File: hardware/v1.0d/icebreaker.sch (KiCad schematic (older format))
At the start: 133 parts, among them J1 Jumper, J10 Jumper, J11 Jumper, J12 Jumper, J13 Jumper, J14 Jumper, J15 Jumper, J16 Jumper, J17 Jumper, J18 Jumper, J19 Jumper, J2 Jumper, J20 Flash, J21 PMOD, J22 PMOD, J23 PMOD, J24 PMOD, J25 RGB Led, J26 5V AUX, J27 5V AUX, J28 CRESET, J29 Jumper, J3 Jumper, J30 Jumper, J31 RGB Led, J32 WS2812, J33 RGB Led, J34 SADD, J4 Jumper, J5 Jumper, J6 Jumper, J7 Jumper, J8 Jumper, J9 Jumper, P1 pkl_USB_OTG, P2 UP, P3 UP, P4 UP, P5 UP, P6 RAM_CS, Q1 BSS138, SW1 TACT, SW2 TACT, SW3 TACT, SW4 TACT, U1 93C46B-SOT-23-6, U2 3.3V, U3 1V2, U4 FT2232H, U5 W25Q, U6 ICE5LP4K-SG48, U7 12MHz

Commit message: Fixed RGB LED labling. Replaced RGB LED signals to be color agnostic.
The FPGA does not care which color is connected to which pin, so
referring to the pins as red, green and blue is bit silly. The signals
are now RGB0-2 instead. The only place where we label the colors are on
the actual Cree LED package pins.

This fixes #22
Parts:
- D11: symbol Device:LED_RGB -> pkl_device:LED_BGR; MFN (none) -> CLX6F-FKC; Manufacturer (none) -> Cree
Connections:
- net ~LED_BLU renamed ~LED_RGB0
- net ~LED_GRN renamed ~LED_RGB1
- net ~LED_RED renamed ~LED_RGB2
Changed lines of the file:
@@
 	10600 4100 10800 4100
 Text Label 10800 4100 0    50   ~ 0
-~LED_BLU
+~LED_RGB0
 Text Label 10800 4000 0    50   ~ 0
-~LED_GRN
+~LED_RGB1
 Text Label 10800 3900 0    50   ~ 0
-~LED_RED
+~LED_RGB2
 Text Notes 600  1700 0    100  ~ 0
 FTDI Programmer/UART/FIFO
@@
 Wire Wire Line
 	14700 8600 14300 8600
-Text Label 15600 8600 0    50   ~ 0
-~LED_RED
 Text Label 14300 8600 2    50   ~ 0
-~LED_GRN
+~LED_RGB1
+Text Label 15600 8600 0    50   ~ 0
+~LED_RGB2
 Text Label 15600 8700 0    50   ~ 0
-~LED_BLU
+~LED_RGB0
 Wire Wire Line
 	13300 4400 13500 4400
@@
 RAM CS
 $Comp
-L Device:LED_RGB D11
+L pkl_device:LED_BGR D11
 U 1 1 5C0C5D9F
 P 14950 9500
@@
 F 3 "~" H 14950 9450 50  0001 C CNN
 F 4 "YES" H 14950 9500 50  0001 C CNN "DNP"
+F 5 "Cree" H 14950 9500 50  0001 C CNN "Manufacturer"
+F 6 "CLX6F-FKC" H 14950 9500 50  0001 C CNN "MFN"
 	1    14950 9500
 	-1   0    0    -1
@@
 	15150 9700 15250 9700
 Text Label 15250 9300 0    50   ~ 0
-~LED_RED
+~LED_RGB2
 Text Label 15250 9500 0    50   ~ 0
-~LED_GRN
+~LED_RGB1
 Text Label 15250 9700 0    50   ~ 0
-~LED_BLU
+~LED_RGB0
 $Comp
 L pkl_misc:pkl_double_jumper_ncno J30

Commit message: Changed the VPP_2V5 diode footprint to SOD-523.
The SOD-523 is more common. While I was at it I also named the VPP_2V5
net.

This fixes #26
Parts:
- D2: value CDBU0520 -> ~~800mVf; footprint pkl_dipol:D_0603 -> pkl_dipol:D_SOD-523; Key diode-schottky-0603 -> diode-schottky-sod523
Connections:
- net VPP_2V5: now reaches C35.1, D2.C, U6.24 (VPP_2V5)
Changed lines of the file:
@@
 Text Label 10700 5700 0    50   ~ 0
 iCE_CRESET
-$Comp
-L pkl_device:pkl_Diode_Small D2
-U 1 1 5A83A5CC
-P 8150 5800
-F 0 "D2" H 8050 5750 50  0000 C CNN
-F 1 "CDBU0520" H 8400 5850 50  0000 C CNN
-F 2 "pkl_dipol:D_0603" V 8150 5800 60  0001 C CNN
-F 3 "" V 8150 5800 60  0000 C CNN
-F 4 "diode-schottky-0603" H 0   0   50  0001 C CNN "Key"
-F 5 "ANY" H 8150 5800 50  0001 C CNN "Source"
-	1    8150 5800
-	1    0    0    -1
-$EndComp
 Wire Wire Line
 	8250 5800 8350 5800
@@
 Text Notes 15250 9850 0    75   ~ 0
 Unpopulated
+$Comp
+L pkl_device:pkl_Diode_Small D2
+U 1 1 5A83A5CC
+P 8150 5800
+F 0 "D2" H 8000 5750 50  0000 L CNN
+F 1 "~~800mVf" H 8000 5650 50  0000 L CNN
+F 2 "pkl_dipol:D_SOD-523" V 8150 5800 60  0001 C CNN
+F 3 "" V 8150 5800 60  0000 C CNN
+F 4 "diode-schottky-sod523" H 0   0   50  0001 C CNN "Key"
+F 5 "ANY" H 8150 5800 50  0001 C CNN "Source"
+	1    8150 5800
+	1    0    0    -1
+$EndComp
+Text Label 8600 5800 2    50   ~ 0
+VPP_2V5
 $EndSCHEMATC

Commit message: Corrected the SAO/I2C ear name in schematic and on board.
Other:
- note added: "SAO/I2C "Ear""
- note removed: "SADD "Ear""
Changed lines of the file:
@@
 WS2812 "Ear"
 Text Notes 9600 10200 0    100  ~ 0
-SADD "Ear"
+SAO/I2C "Ear"
 Wire Notes Line
 	9500 10000 11700 10000

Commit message: Changed the AUX CS jumper to be Normally Closed.
This closes #28
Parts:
- J29: footprint pkl_jumpers:J_0603 -> pkl_jumpers:J_NC_0603_15; symbol pkl_misc:pkl_jumper -> pkl_misc:pkl_jumper_nc
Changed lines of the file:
@@
 $EndComp
 $Comp
-L pkl_misc:pkl_jumper J29
+L pkl_misc:pkl_jumper_nc J29
 U 1 1 5BF627F5
 P 5600 3550
 F 0 "J29" H 5450 3600 60  0000 C CNN
 F 1 "Jumper" H 5600 3695 60  0001 C CNN
-F 2 "pkl_jumpers:J_0603" H 5600 3550 60  0001 C CNN
+F 2 "pkl_jumpers:J_NC_0603_15" H 5600 3550 60  0001 C CNN
 F 3 "" H 5600 3550 60  0000 C CNN
 F 4 "ANY" H 5600 3550 50  0001 C CNN "Source"

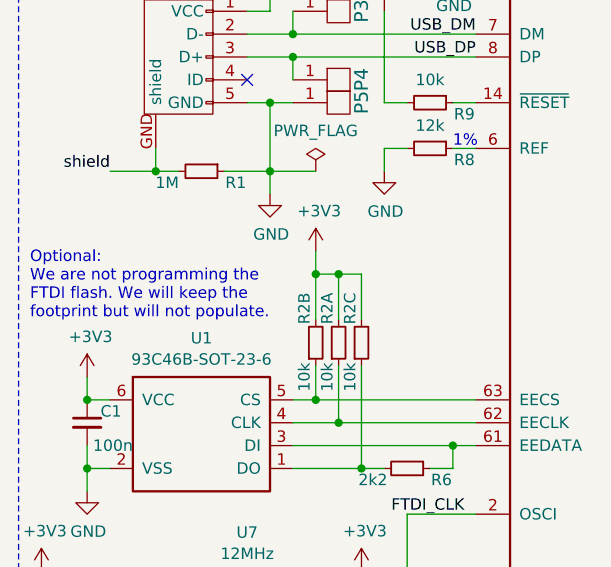
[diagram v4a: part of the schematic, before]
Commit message: Corrected the note about FTDI Flash.
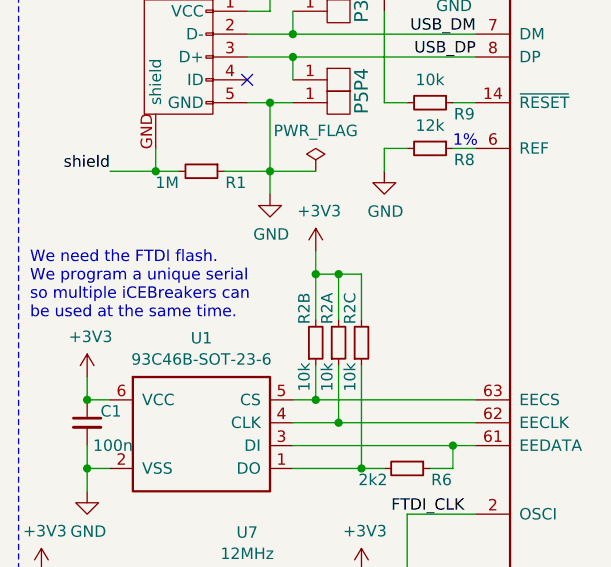
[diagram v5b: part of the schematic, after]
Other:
- note added: "We need the FTDI flash.\nWe program a unique serial\nso multiple iCEBreakers can\nbe used at the same time."
- note removed: "Optional:\nWe are not programming the\nFTDI flash. We will keep the\nfootprint but will not populate."
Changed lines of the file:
@@
 Wire Wire Line
 	5800 6750 5800 7050
-Text Notes 550  5500 0    50   ~ 0
-Optional:\nWe are not programming the\nFTDI flash. We will keep the\nfootprint but will not populate.
 $Comp
 L pkl_device:pkl_R_Small R26
@@
 Text Label 8600 5800 2    50   ~ 0
 VPP_2V5
+Text Notes 550  5500 0    50   ~ 0
+We need the FTDI flash.\nWe program a unique serial\nso multiple iCEBreakers can\nbe used at the same time.
 $EndSCHEMATC

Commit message: Some more minor cleanups.
* Renamed ear data nets to match the RGB connector signal numbering
* Added graphics to make it clearer where the ear labels belong to
* Moved the 3v3 regulator via to increase the space between via drill
  hits
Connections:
- net EB_OD1: now also J33.1 (Pin_1), J34.4 (Pin_4), R29.1; no longer J33.2 (Pin_2), J34.2 (Pin_2), R28.1
- net EB_OD2: now also J33.2 (Pin_2), J34.2 (Pin_2), R28.1; no longer J33.1 (Pin_1), J34.4 (Pin_4), R29.1
- net ET_OD1: now also J31.1 (Pin_1); no longer J31.2 (Pin_2), Q1.1 (G), R7.2
- net ET_OD2: now also J31.2 (Pin_2), Q1.1 (G), R7.2; no longer J31.1 (Pin_1)
- net EB_OD3 renamed EB_OD0
- net ET_O1 renamed ET_O2
- net ET_OD3 renamed ET_OD0
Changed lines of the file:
@@
 	7400 10400 7300 10400
 Text Label 8000 10400 0    50   ~ 0
+ET_OD2
+Text Label 7300 10400 2    50   ~ 0
 ET_OD1
-Text Label 7300 10400 2    50   ~ 0
-ET_OD2
 Text Label 8000 10500 0    50   ~ 0
-ET_OD3
+ET_OD0
 Wire Wire Line
 	7300 10600 7400 10600
@@
 Connection ~ 8700 10800
 Text Label 8600 10800 2    50   ~ 0
-ET_OD1
+ET_OD2
 Wire Wire Line
 	8600 10300 8700 10300
@@
 Connection ~ 9000 11100
 Text Label 9000 10500 2    50   ~ 0
-ET_O1
+ET_O2
 $Comp
 L Connector_Generic:Conn_02x04_Odd_Even J33
@@
 	9900 10400 9800 10400
 Text Label 10500 10400 0    50   ~ 0
+EB_OD2
+Text Label 9800 10400 2    50   ~ 0
 EB_OD1
-Text Label 9800 10400 2    50   ~ 0
-EB_OD2
 Text Label 10500 10500 0    50   ~ 0
-EB_OD3
+EB_OD0
 Wire Wire Line
 	9800 10600 9900 10600
@@
 Connection ~ 11300 11000
 Text Label 11400 10900 0    50   ~ 0
+EB_OD2
+Text Label 11400 11000 0    50   ~ 0
 EB_OD1
-Text Label 11400 11000 0    50   ~ 0
-EB_OD2
 Text Notes 7100 10200 0    100  ~ 0
 WS2812 "Ear"
